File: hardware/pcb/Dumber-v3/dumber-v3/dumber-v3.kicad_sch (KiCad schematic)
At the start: 0 parts

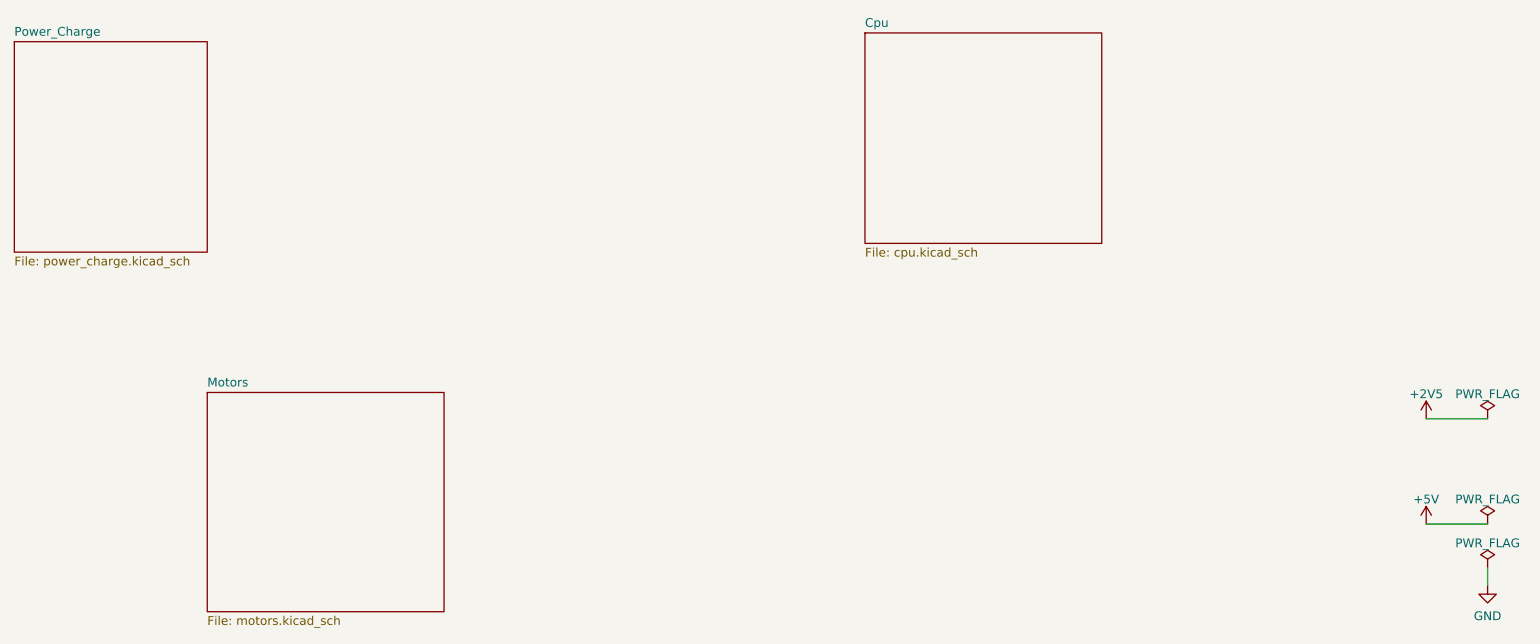
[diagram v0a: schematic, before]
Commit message: Schema complet, projet logiciel demarré
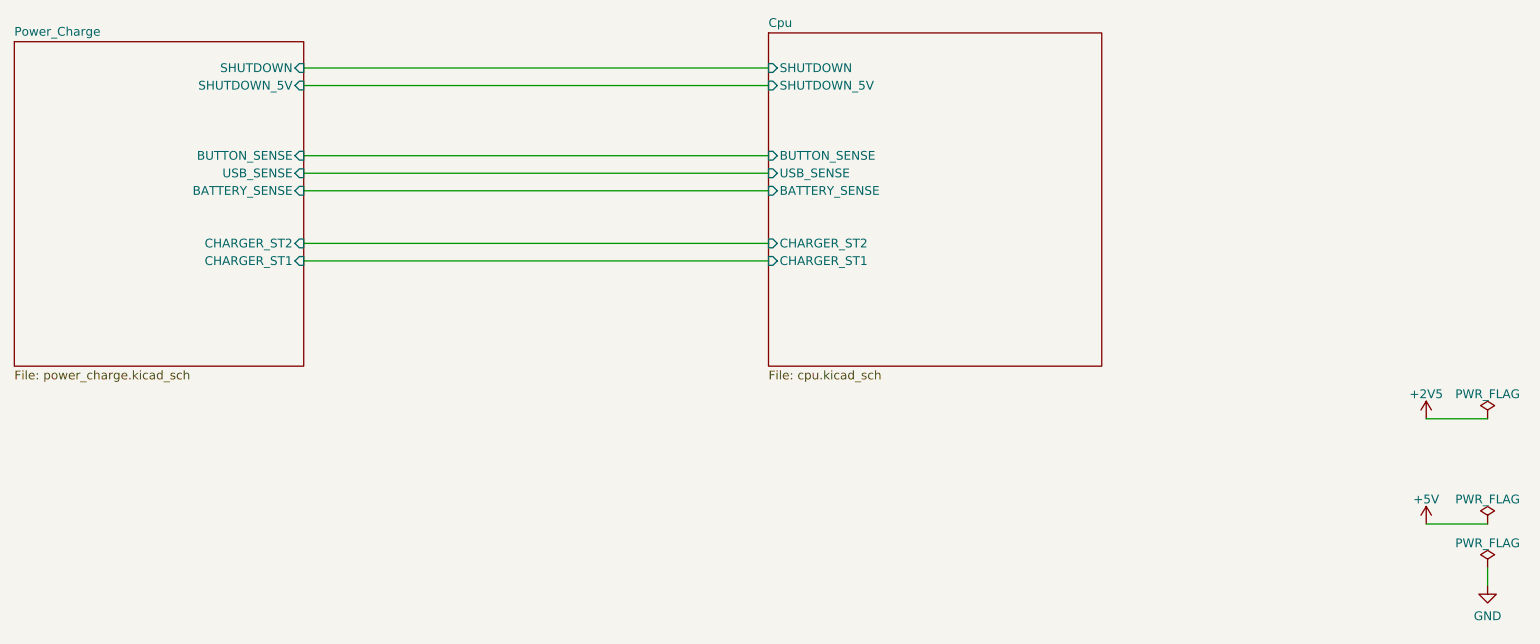
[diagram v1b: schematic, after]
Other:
- removed sheet Motors
- sheet Cpu ports: added BATTERY_SENSE, BUTTON_SENSE, CHARGER_ST1, CHARGER_ST2, SHUTDOWN, SHUTDOWN_5V, USB_SENSE; removed none
- sheet Power_Charge ports: added BATTERY_SENSE, BUTTON_SENSE, CHARGER_ST1, CHARGER_ST2, SHUTDOWN, SHUTDOWN_5V, USB_SENSE; removed none

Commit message: PCB fini
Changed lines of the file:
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@@
-    (stroke (width 0) (type default) (color 0 0 0 0))
-  )
-  (wire (pts (xy 252.73 91.44) (xy 261.62 91.44))
     (stroke (width 0) (type default) (color 0 0 0 0))
   )
@@
     (pin "1")
   )
-  (symbol (lib_id "power:+2V5") (at 252.73 91.44 0) (unit 1)
-    (in_bom yes) (on_board yes) (fields_autoplaced)
-    (property "Reference" "#PWR01" (id 0) (at 252.73 95.25 0)
-      (effects (font (size 1.27 1.27)) hide)
-    )
-    (property "Value" "+2V5" (id 1) (at 252.73 87.8642 0))
-    (property "Footprint" "" (id 2) (at 252.73 91.44 0)
-      (effects (font (size 1.27 1.27)) hide)
-    )
-    (property "Datasheet" "" (id 3) (at 252.73 91.44 0)
-      (effects (font (size 1.27 1.27)) hide)
-    )
-    (pin "1")
-  )
   (symbol (lib_id "power:PWR_FLAG") (at 261.62 106.68 0) (unit 1)
     (in_bom yes) (on_board yes) (fields_autoplaced)
@@
     )
     (property "Datasheet" "~" (id 3) (at 261.62 106.68 0)
-      (effects (font (size 1.27 1.27)) hide)
-    )
-    (pin "1")
-  )
-  (symbol (lib_id "power:PWR_FLAG") (at 261.62 91.44 0) (unit 1)
-    (in_bom yes) (on_board yes) (fields_autoplaced)
-    (property "Reference" "#FLG01" (id 0) (at 261.62 89.535 0)
-      (effects (font (size 1.27 1.27)) hide)
-    )
-    (property "Value" "PWR_FLAG" (id 1) (at 261.62 87.8642 0))
-    (property "Footprint" "" (id 2) (at 261.62 91.44 0)
-      (effects (font (size 1.27 1.27)) hide)
-    )
-    (property "Datasheet" "~" (id 3) (at 261.62 91.44 0)
       (effects (font (size 1.27 1.27)) hide)
     )
@@
   )
   (symbol_instances
-    (path "/d64fd0ea-fc82-433a-963a-a73afec532ec"
-      (reference "#FLG01") (unit 1) (value "PWR_FLAG") (footprint "")
-    )
     (path "/8ff646fb-419a-4551-946a-0a931ac2f006"
       (reference "#FLG03") (unit 1) (value "PWR_FLAG") (footprint "")
@@
       (reference "#FLG0102") (unit 1) (value "PWR_FLAG") (footprint "")
     )
-    (path "/8f482ed0-fa5b-4e0a-9bcf-58db7d86f2a1"
-      (reference "#PWR01") (unit 1) (value "+2V5") (footprint "")
-    )
     (path "/3615d78e-1dd3-4b20-9017-3539b8f88e06/fd167bd0-441b-451a-a5e1-0aab203dc3d4"
       (reference "#PWR02") (unit 1) (value "+2V5") (footprint "")
@@
       (reference "#PWR0104") (unit 1) (value "GND") (footprint "")
     )
+    (path "/1b100198-bac5-4efe-bc54-3b6ec493e580/ea8a6096-ab5d-4cb8-a1df-44b4d0dbf6ba"
+      (reference "#PWR0105") (unit 1) (value "GND") (footprint "")
+    )
     (path "/1b100198-bac5-4efe-bc54-3b6ec493e580/26ead04d-d956-4295-9020-a08b69be4277"
       (reference "#PWR0106") (unit 1) (value "GND") (footprint "")
@@
       (reference "#PWR0108") (unit 1) (value "+2V5") (footprint "")
     )
+    (path "/1b100198-bac5-4efe-bc54-3b6ec493e580/7bee68da-e7ef-4a18-b224-5e09bc40a3bd"
+      (reference "#PWR0109") (unit 1) (value "+2V5") (footprint "")
+    )
     (path "/3615d78e-1dd3-4b20-9017-3539b8f88e06/053dd8a9-6683-412e-b95b-646ea38b2cad"
       (reference "BT1") (unit 1) (value "Li-ION") (footprint "Battery:BatteryHolder_Keystone_2460_1xAA")
@@
     )
     (path "/1b100198-bac5-4efe-bc54-3b6ec493e580/3b6b3612-3075-4103-a4ca-2af50c36e62f"
-      (reference "C12") (unit 1) (value "C") (footprint "Capacitor_SMD:C_0805_2012Metric")
+      (reference "C12") (unit 1) (value "1µF") (footprint "Capacitor_SMD:C_0805_2012Metric")
     )
     (path "/1b100198-bac5-4efe-bc54-3b6ec493e580/4ea93de4-5e17-4d11-b46b-d6ff189af8c9"
-      (reference "C13") (unit 1) (value "C") (footprint "Capacitor_SMD:C_0805_2012Metric")
+      (reference "C13") (unit 1) (value "1µF") (footprint "Capacitor_SMD:C_0805_2012Metric")
     )
     (path "/1b100198-bac5-4efe-bc54-3b6ec493e580/15085dfc-47f4-4f8e-8b33-010f139cbd2e"
-      (reference "C14") (unit 1) (value "C") (footprint "Capacitor_SMD:C_0805_2012Metric")
+      (reference "C14") (unit 1) (value "470nF") (footprint "Capacitor_SMD:C_0805_2012Metric")
     )
     (path "/1b100198-bac5-4efe-bc54-3b6ec493e580/3f85c904-e97d-4be1-a718-e5c6add66c0a"
-      (reference "C15") (unit 1) (value "C") (footprint "Capacitor_SMD:C_0805_2012Metric")
+      (reference "C15") (unit 1) (value "470nF") (footprint "Capacitor_SMD:C_0805_2012Metric")
     )
     (path "/1b100198-bac5-4efe-bc54-3b6ec493e580/5c6cbf4a-879f-44a0-95ad-6088994ddad8"
       (reference "C16") (unit 1) (value "100nF") (footprint "Capacitor_SMD:C_0805_2012Metric")
     )
+    (path "/1b100198-bac5-4efe-bc54-3b6ec493e580/3d7147e1-c45f-4241-a086-49e65ede1cfc"
+      (reference "C17") (unit 1) (value "100nF") (footprint "Capacitor_SMD:C_0805_2012Metric")
+    )
+    (path "/1b100198-bac5-4efe-bc54-3b6ec493e580/dc12807b-c3e2-45ed-bc8b-70aa2a59fa1d"
+      (reference "C18") (unit 1) (value "100nF") (footprint "Capacitor_SMD:C_0805_2012Metric")
+    )
+    (path "/1b100198-bac5-4efe-bc54-3b6ec493e580/98c4472a-5e03-44c4-9716-29e540c0c9a8"
+      (reference "C19") (unit 1) (value "100nF") (footprint "Capacitor_SMD:C_0805_2012Metric")
+    )
+    (path "/1b100198-bac5-4efe-bc54-3b6ec493e580/5ac179f3-da22-4fda-a42d-23a6caf2906d"
+      (reference "C20") (unit 1) (value "100nF") (footprint "Capacitor_SMD:C_0805_2012Metric")
+    )
     (path "/3615d78e-1dd3-4b20-9017-3539b8f88e06/d735c11c-af51-402c-bf6b-5022004af723"
       (reference "D1") (unit 1) (value "PMEG2020CPA") (footprint "INSA:Nexperia_SOT-1061")
@@
     )
     (path "/1b100198-bac5-4efe-bc54-3b6ec493e580/5adf52fb-af5a-46ac-94b1-da31d840abc2"
-      (reference "R16") (unit 1) (value "R") (footprint "Resistor_SMD:R_0805_2012Metric")
+      (reference "R16") (unit 1) (value "1.5K") (footprint "Resistor_SMD:R_0805_2012Metric")
     )
     (path "/3615d78e-1dd3-4b20-9017-3539b8f88e06/6d0a8559-6806-445a-9150-dfd0496b6eb9"
@@
     )
     (path "/1b100198-bac5-4efe-bc54-3b6ec493e580/6584e4cf-80fd-476b-ad9c-e381729bd6ab"
-      (reference "R22") (unit 1) (value "R") (footprint "Resistor_SMD:R_0805_2012Metric")
+      (reference "R22") (unit 1) (value "1.5K") (footprint "Resistor_SMD:R_0805_2012Metric")
     )
     (path "/1b100198-bac5-4efe-bc54-3b6ec493e580/97d27f4c-b224-4415-b3b6-33cbd34be51c"
-      (reference "R23") (unit 1) (value "R") (footprint "Resistor_SMD:R_0805_2012Metric")
+      (reference "R23") (unit 1) (value "1.5K") (footprint "Resistor_SMD:R_0805_2012Metric")
     )
     (path "/1b100198-bac5-4efe-bc54-3b6ec493e580/b6914fe2-614d-400f-b838-b498fec4ecdb"

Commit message: Mise a jour PCB et coque. Des fichiers STEP ne sont pas encore remontés car trop gros
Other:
- sheet Cpu ports: added BUTTON_PRESS; removed none
- sheet Power_Charge ports: added BUTTON_PRESS; removed none
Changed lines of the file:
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@@
+    (stroke (width 0) (type default) (color 0 0 0 0))
+  )
+  (wire (pts (xy 90.17 76.2) (xy 157.48 76.2))
     (stroke (width 0) (type default) (color 0 0 0 0))
   )
@@
       (effects (font (size 1.27 1.27)) (justify left))
     )
+    (pin "BUTTON_PRESS" input (at 157.48 76.2 180)
+      (effects (font (size 1.27 1.27)) (justify left))
+    )
   )
   (sheet (at 48.26 36.83) (size 41.91 46.99) (fields_autoplaced)
@@
       (effects (font (size 1.27 1.27)) (justify right))
     )
+    (pin "BUTTON_PRESS" input (at 90.17 76.2 0)
+      (effects (font (size 1.27 1.27)) (justify right))
+    )
   )
   (sheet_instances
@@
       (reference "#PWR026") (unit 1) (value "GND") (footprint "")
     )
+    (path "/1b100198-bac5-4efe-bc54-3b6ec493e580/348bff38-f368-4df7-8c1c-5a82d78f9145"
+      (reference "#PWR027") (unit 1) (value "GND") (footprint "")
+    )
     (path "/1b100198-bac5-4efe-bc54-3b6ec493e580/6f9a5a58-ab28-4346-bc05-af16f57c158d"
       (reference "#PWR028") (unit 1) (value "GND") (footprint "")
@@
       (reference "#PWR0101") (unit 1) (value "GND") (footprint "")
     )
-    (path "/1b100198-bac5-4efe-bc54-3b6ec493e580/b80c41d6-36c3-46db-817a-33249c16cc41"
-      (reference "#PWR0102") (unit 1) (value "GND") (footprint "")
-    )
     (path "/1b100198-bac5-4efe-bc54-3b6ec493e580/1f8703f8-4e55-4f9a-88f5-f5ae70adabfd"
       (reference "#PWR0103") (unit 1) (value "+2V5") (footprint "")
@@
     )
     (path "/3615d78e-1dd3-4b20-9017-3539b8f88e06/290b23d2-ab07-4d64-ad75-994bc73cc28d"
-      (reference "C5") (unit 1) (value "100nF") (footprint "Capacitor_SMD:C_0805_2012Metric")
+      (reference "C5") (unit 1) (value "2.2µF") (footprint "Capacitor_SMD:C_0805_2012Metric")
     )
     (path "/3615d78e-1dd3-4b20-9017-3539b8f88e06/b05e8c1b-5e98-418d-98a2-eb692cc0123e"
@@
       (reference "C7") (unit 1) (value "1µF") (footprint "Capacitor_SMD:C_0805_2012Metric")
     )
-    (path "/3615d78e-1dd3-4b20-9017-3539b8f88e06/db04ab93-6753-4375-baed-64e74f12496d"
-      (reference "C8") (unit 1) (value "100µF") (footprint "Capacitor_SMD:C_1210_3225Metric")
+    (path "/3615d78e-1dd3-4b20-9017-3539b8f88e06/d7ec8307-042b-4921-9b77-d9ed100664d8"
+      (reference "C8") (unit 1) (value "650pF") (footprint "Capacitor_SMD:C_0805_2012Metric")
     )
     (path "/3615d78e-1dd3-4b20-9017-3539b8f88e06/16366f03-a170-4809-ab0e-52a609d8b01f"
@@
     )
     (path "/3615d78e-1dd3-4b20-9017-3539b8f88e06/a63b8def-5f1b-4d9d-bb74-90ccd6d05047"
-      (reference "C10") (unit 1) (value "100µF") (footprint "Capacitor_SMD:C_1210_3225Metric")
+      (reference "C10") (unit 1) (value "10µF") (footprint "Capacitor_SMD:C_1210_3225Metric")
     )
     (path "/3615d78e-1dd3-4b20-9017-3539b8f88e06/707c32d4-4845-4691-92d6-ca54beed384c"
@@
       (reference "D2") (unit 1) (value "FM5818-W") (footprint "Diode_SMD:D_SMA")
     )
-    (path "/1b100198-bac5-4efe-bc54-3b6ec493e580/4f3676d7-89bb-4e10-b37e-c3a10196c6f0"
-      (reference "D3") (unit 1) (value "LED") (footprint "Diode_SMD:D_0805_2012Metric")
-    )
-    (path "/1b100198-bac5-4efe-bc54-3b6ec493e580/43b03800-061e-478b-951c-e250eeb41dcb"
-      (reference "D4") (unit 1) (value "LED") (footprint "Diode_SMD:D_0805_2012Metric")
-    )
-    (path "/1b100198-bac5-4efe-bc54-3b6ec493e580/8520db94-9efd-4100-800f-4f7e9a13252a"
-      (reference "D5") (unit 1) (value "LED") (footprint "Diode_SMD:D_0805_2012Metric")
+    (path "/3615d78e-1dd3-4b20-9017-3539b8f88e06/70931bb2-f30a-426f-8190-d5c89b5e8222"
+      (reference "H1") (unit 1) (value "MountingHole") (footprint "MountingHole:MountingHole_3.2mm_M3_ISO14580")
+    )
+    (path "/3615d78e-1dd3-4b20-9017-3539b8f88e06/318ca598-5b82-4017-94b2-876608dcab97"
+      (reference "H2") (unit 1) (value "MountingHole") (footprint "MountingHole:MountingHole_3.2mm_M3_ISO14580")
+    )
+    (path "/3615d78e-1dd3-4b20-9017-3539b8f88e06/fc812e6a-40f4-4cb6-9945-123fe42fd4ff"
+      (reference "H3") (unit 1) (value "MountingHole") (footprint "MountingHole:MountingHole_3.2mm_M3_ISO14580")
     )
     (path "/1b100198-bac5-4efe-bc54-3b6ec493e580/ad90e2d3-97b9-46c2-8dd0-1f06ea84ef6b"
@@
     )
     (path "/1b100198-bac5-4efe-bc54-3b6ec493e580/eb3899c1-5b12-45e0-8c00-fdefc61483aa"
-      (reference "J3") (unit 1) (value "Conn_02x05_Odd_Even") (footprint "Connector_PinHeader_1.27mm:PinHeader_2x05_P1.27mm_Vertical_SMD")
-    )
-    (path "/3615d78e-1dd3-4b20-9017-3539b8f88e06/ae93d87b-a48e-48be-af7f-711e740d7cdc"
-      (reference "L2") (unit 1) (value "22µH") (footprint "Inductor_SMD:L_Taiyo-Yuden_MD-4040")
+      (reference "J3") (unit 1) (value "Conn_02x05_Odd_Even") (footprint "Connector_PinHeader_1.27mm:PinHeader_2x05_P1.27mm_Horizontal")
+    )
+    (path "/1b100198-bac5-4efe-bc54-3b6ec493e580/d9436e2a-adfe-4a85-b564-02e5a41ce103"
+      (reference "J4") (unit 1) (value "TE 1-84982-0") (footprint "INSA:TE 1-84982-0")
+    )
+    (path "/3615d78e-1dd3-4b20-9017-3539b8f88e06/cb35137a-a8ed-4480-a7e1-1f175bdf4bd3"
+      (reference "L1") (unit 1) (value "10µH") (footprint "Inductor_SMD:L_Bourns_SRP7028A_7.3x6.6mm")
     )
     (path "/1b100198-bac5-4efe-bc54-3b6ec493e580/b8ba459f-4564-488d-a7fd-fbd97b4a8b51"
@@
     )
     (path "/3615d78e-1dd3-4b20-9017-3539b8f88e06/58ee17a8-90a8-405f-9a19-8126994f76ff"
-      (reference "R8") (unit 1) (value "5K") (footprint "Resistor_SMD:R_0805_2012Metric")
+      (reference "R8") (unit 1) (value "47K") (footprint "Resistor_SMD:R_0805_2012Metric")
     )
     (path "/3615d78e-1dd3-4b20-9017-3539b8f88e06/0ea2454f-b423-4f55-8c11-36db50920ffb"
@@
     )
     (path "/3615d78e-1dd3-4b20-9017-3539b8f88e06/e257cddb-a9e9-4642-b7b3-1ba1238ca42a"
-      (reference "R10") (unit 1) (value "3.72K") (footprint "Resistor_SMD:R_0805_2012Metric")
+      (reference "R10") (unit 1) (value "40.2K") (footprint "Resistor_SMD:R_0805_2012Metric")
     )
     (path "/3615d78e-1dd3-4b20-9017-3539b8f88e06/f13b9b51-766a-4b76-a09c-958c9da8f460"
-      (reference "R11") (unit 1) (value "1.28K") (footprint "Resistor_SMD:R_0805_2012Metric")
+      (reference "R11") (unit 1) (value "13.3K") (footprint "Resistor_SMD:R_0805_2012Metric")
     )
     (path "/3615d78e-1dd3-4b20-9017-3539b8f88e06/da5fc659-2f73-4499-97f7-301d8bfb0ffa"
@@
       (reference "R15") (unit 1) (value "1M") (footprint "Resistor_SMD:R_0805_2012Metric")
     )
-    (path "/1b100198-bac5-4efe-bc54-3b6ec493e580/5adf52fb-af5a-46ac-94b1-da31d840abc2"
-      (reference "R16") (unit 1) (value "1K") (footprint "Resistor_SMD:R_0805_2012Metric")
-    )
     (path "/3615d78e-1dd3-4b20-9017-3539b8f88e06/6d0a8559-6806-445a-9150-dfd0496b6eb9"
       (reference "R17") (unit 1) (value "150K") (footprint "Resistor_SMD:R_0805_2012Metric")
@@
       (reference "R20") (unit 1) (value "100K") (footprint "Resistor_SMD:R_0805_2012Metric")
     )
-    (path "/1b100198-bac5-4efe-bc54-3b6ec493e580/6584e4cf-80fd-476b-ad9c-e381729bd6ab"
-      (reference "R22") (unit 1) (value "1K") (footprint "Resistor_SMD:R_0805_2012Metric")
-    )
-    (path "/1b100198-bac5-4efe-bc54-3b6ec493e580/97d27f4c-b224-4415-b3b6-33cbd34be51c"
-      (reference "R23") (unit 1) (value "820") (footprint "Resistor_SMD:R_0805_2012Metric")
-    )
     (path "/1b100198-bac5-4efe-bc54-3b6ec493e580/b6914fe2-614d-400f-b838-b498fec4ecdb"
       (reference "R24") (unit 1) (value "100K") (footprint "Resistor_SMD:R_0805_2012Metric")
@@
       (reference "R29") (unit 1) (value "100K") (footprint "Resistor_SMD:R_0805_2012Metric")
     )
+    (path "/1b100198-bac5-4efe-bc54-3b6ec493e580/46e1af65-a5a2-45d4-b579-71945968a939"
+      (reference "RN1") (unit 1) (value "1K") (footprint "Resistor_SMD:R_Array_Convex_4x1206")
+    )
+    (path "/1b100198-bac5-4efe-bc54-3b6ec493e580/0f814362-f7f7-453e-8fb8-eef7cc06aa18"
+      (reference "RN2") (unit 1) (value "1K") (footprint "Resistor_SMD:R_Array_Convex_4x1206")
+    )
     (path "/3615d78e-1dd3-4b20-9017-3539b8f88e06/a2307e07-4a0e-45a0-860c-02d4c012955d"
       (reference "SW1") (unit 1) (value "SW_Push") (footprint "Button_Switch_SMD:Panasonic_EVQPUJ_EVQPUA")
@@
       (reference "U2") (unit 1) (value "STM32F071CBTx") (footprint "Package_QFP:LQFP-48_7x7mm_P0.5mm")
     )
-    (path "/3615d78e-1dd3-4b20-9017-3539b8f88e06/d1632f43-8228-45f5-b90a-b4352f510caf"
+    (path "/3615d78e-1dd3-4b20-9017-3539b8f88e06/1c6e7514-e426-4cb3-922e-1293285c7252"
       (reference "U3") (unit 1) (value "LTC2954-2") (footprint "Package_TO_SOT_SMD:SOT-23-8")
     )
@@
       (reference "U4") (unit 1) (value "L6924U") (footprint "INSA:L6924UTR")
     )
-    (path "/3615d78e-1dd3-4b20-9017-3539b8f88e06/ddc88c6d-c225-4696-8d58-9df99940fc57"
-      (reference "U5") (unit 1) (value "NCV5171") (footprint "Package_SO:SO-8_3.9x4.9mm_P1.27mm")
+    (path "/3615d78e-1dd3-4b20-9017-3539b8f88e06/0bc43163-613d-49e2-b443-50b6bf7d3320"
+      (reference "U5") (unit 1) (value "LM2731XMF") (footprint "Package_TO_SOT_SMD:SOT-23-5")
     )
     (path "/3615d78e-1dd3-4b20-9017-3539b8f88e06/fa604296-bc37-4ba5-96fe-4590ffd6650e"
